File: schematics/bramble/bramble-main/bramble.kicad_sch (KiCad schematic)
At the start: 15 parts, among them Q1 DMN3300U, U1 TDN_5-0910WISM, U2 Opamp_Quad

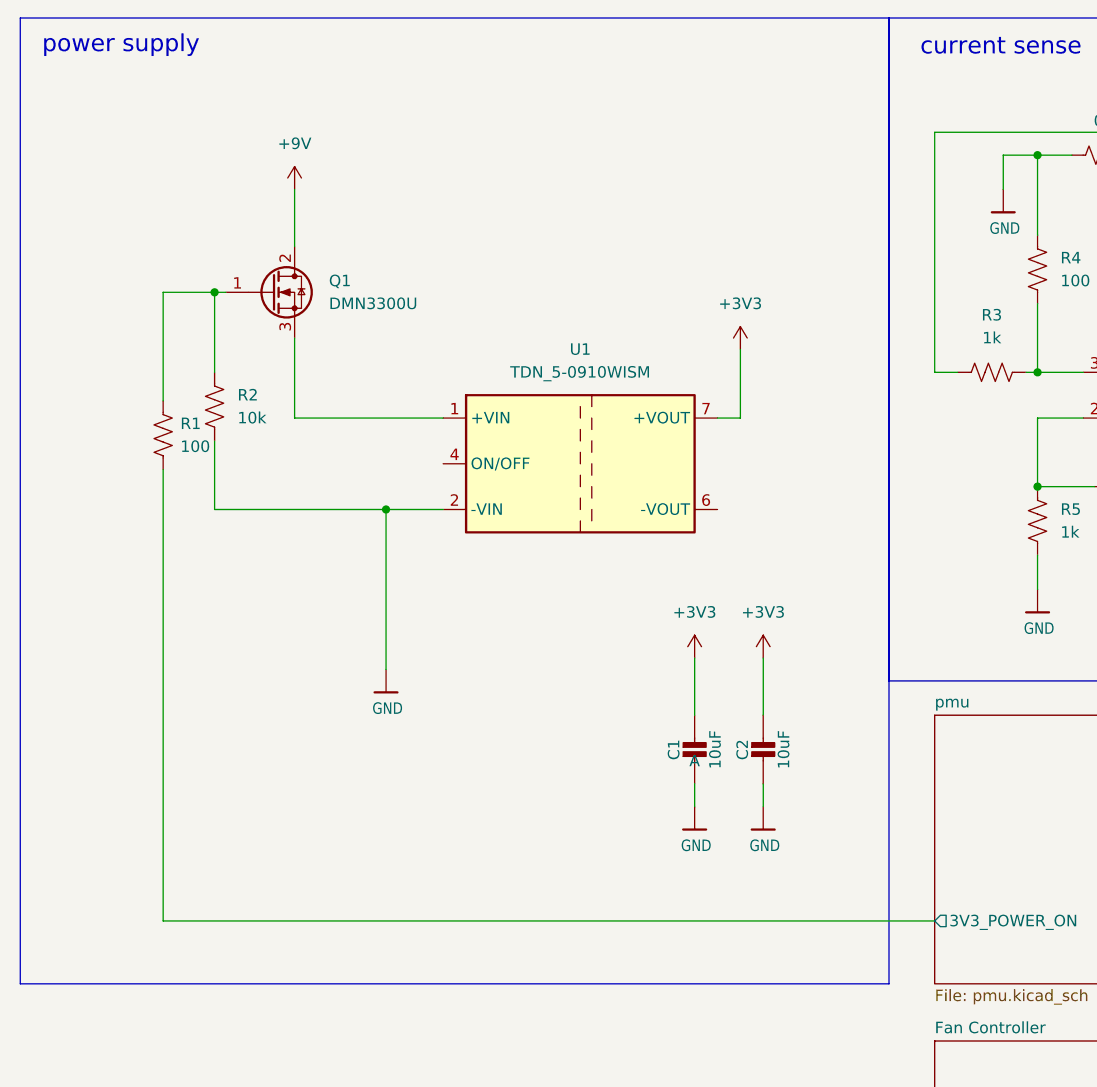
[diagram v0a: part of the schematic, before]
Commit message: fix: swap spi pins, change footprints, etc
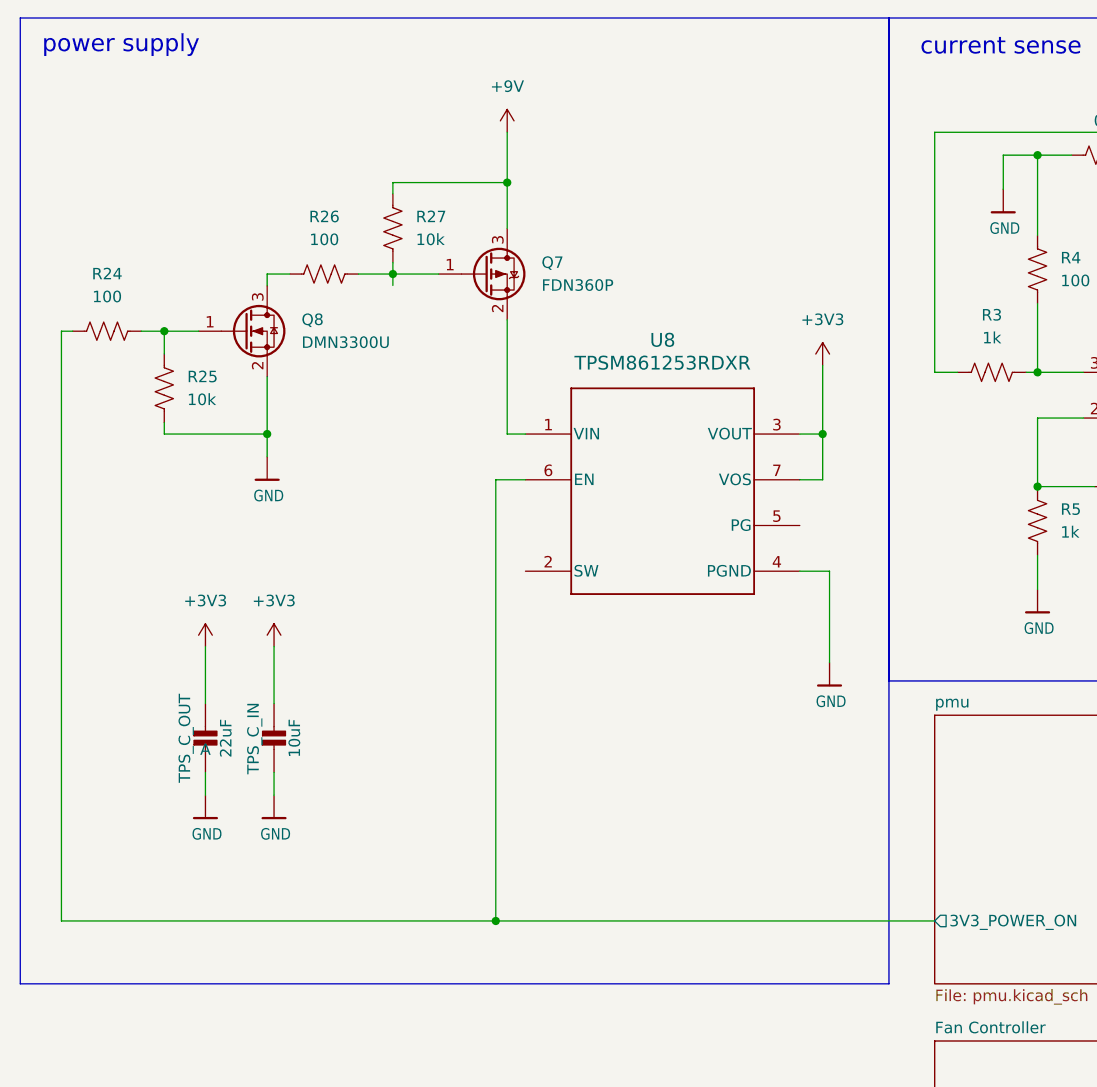
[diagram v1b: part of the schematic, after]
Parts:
- removed Q1: DMN3300U, Package_TO_SOT_SMD:SOT-23, symbol Transistor_FET:DMN3300U
- removed R1: 100, Resistor_SMD:R_0805_2012Metric, symbol Device:R_US
- removed R2: 10k, Resistor_SMD:R_0805_2012Metric, symbol Device:R_US
- removed U1: TDN_5-0910WISM, Converter_DCDC:Converter_DCDC_TRACO_TDN_5-xxxxWISM_SMD, symbol Regulator_Switching:TDN_5-0910WISM
- added Q7: FDN360P, Package_TO_SOT_SMD:SOT-23, symbol Transistor_FET:FDN340P
- added Q8: DMN3300U, Package_TO_SOT_SMD:SOT-23, symbol Transistor_FET:DMN3300U
- added R24: 100, Resistor_SMD:R_0805_2012Metric, symbol Device:R_US
- added R25: 10k, Resistor_SMD:R_0805_2012Metric, symbol Device:R_US
- added R26: 100, Capacitor_SMD:C_0805_2012Metric, symbol Device:R_US
- added R27: 10k, Capacitor_SMD:C_0805_2012Metric, symbol Device:R_US
- added U8: TPSM861253RDXR, RDX0007A-MFG, symbol TPSM861253RDXR:TPSM861253RDXR
- TPS_C_OUT: renamed from C1; value 10uF -> 22uF
- renumbered C2 to TPS_C_IN
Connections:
- net +3V3: now also U8.3 (VOUT), U8.7 (VOS)
- net +9V: now also Q7.3 (D), R27.1
- net GND: now also Q8.2 (S), R25.2, U8.4 (PGND)
- net pmu/3V3_POWER_ON: now also R24.2, U8.6 (EN)
- new net: Q8.1 (G), R24.1, R25.1
- new net: Q8.3 (D), R26.2
- new net: Q7.1 (G), R26.1, R27.2
- new net: Q7.2 (S), U8.1 (VIN)
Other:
- moved on the sheet: TPS_C_IN, TPS_C_OUT

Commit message: pre-fab check-in of v2
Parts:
- removed U8: TPSM861253RDXR, RDX0007A-MFG, symbol TPSM861253RDXR:TPSM861253RDXR
- added VR1: TPSM861253RDXR, Bramble:VREG_TPSM861253RDXR, symbol bramble:TPSM861253RDXR
- R3: renamed from R26; value 100 -> 100k
- renumbered Q8 to Q1, Q7 to Q2, R24 to R1, R8 to R10, R9 to R11, R10 to R12, R25 to R2, R27 to R4, R3 to R5, R4 to R6, R5 to R7, R6 to R8, R7 to R9, TPS_C_IN to TPS_C_IN1, TPS_C_OUT to TPS_C_OUT1
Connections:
- net +3V3: now also VR1.3 (VOUT), VR1.5 (PG)
- net GND: now also VR1.4 (PGND)
- net pmu/3V3_POWER_ON: now also VR1.6 (EN)
- net at Q2.2 (S): now also VR1.1 (VIN)
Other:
- removed sheet Fan Controller

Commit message: Checking before rollback
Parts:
- renumbered U2 to U1
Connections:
- net +3V3: now also VR1.7 (VOS); no longer VR1.5 (PG)
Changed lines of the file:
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@@
 	)
 	(junction
-		(at 31.242 50.038)
+		(at 104.394 61.468)
 		(diameter 0)
 		(color 0 0 0 0)
 	)
 	(junction
-		(at 128.27 67.31)
+		(at 31.242 50.038)
 		(diameter 0)
 		(color 0 0 0 0)
 	)
 	(junction
-		(at 104.394 61.468)
+		(at 128.27 67.31)
 		(diameter 0)
 		(color 0 0 0 0)
@@
 	(wire
 		(pts
-			(xy 203.2 58.42) (xy 199.39 58.42)
+			(xy 101.854 71.628) (xy 104.394 71.628)
 		)
 		(stroke
@@
 	(wire
 		(pts
-			(xy 101.854 61.468) (xy 104.394 61.468)
+			(xy 203.2 58.42) (xy 199.39 58.42)
 		)
 		(stroke
@@
 	(wire
 		(pts
-			(xy 104.394 66.548) (xy 104.394 61.468)
+			(xy 101.854 61.468) (xy 104.394 61.468)
 		)
 		(stroke
@@
 	(wire
 		(pts
+			(xy 104.394 61.468) (xy 104.394 71.628)
+		)
+		(stroke
+			(width 0)
+			(type default)
+		)
+	)
+	(wire
+		(pts
 			(xy 199.39 58.42) (xy 199.39 63.5)
 		)
@@
 	(wire
 		(pts
-			(xy 101.854 66.548) (xy 104.394 66.548)
+			(xy 104.394 53.848) (xy 104.394 61.468)
 		)
 		(stroke
@@
 	(wire
 		(pts
-			(xy 104.394 53.848) (xy 104.394 61.468)
-		)
-		(stroke
-			(width 0)
-			(type default)
-		)
-	)
-	(wire
-		(pts
 			(xy 42.672 61.468) (xy 42.672 64.008)
 		)
@@
 		(dnp no)
 		(fields_autoplaced yes)
-		(property "Reference" "U2"
+		(property "Reference" "U1"
 			(at 274.32 31.75 0)
 			(effects
@@
 			(project ""
 				(path "/e35d7dcf-51bd-456f-89cf-e52d660079b4"
-					(reference "U2")
+					(reference "U1")
 					(unit 3)
 				)
@@
 		(dnp no)
 		(fields_autoplaced yes)
-		(property "Reference" "U2"
+		(property "Reference" "U1"
 			(at 140.97 46.99 0)
 			(effects
@@
 			(project ""
 				(path "/e35d7dcf-51bd-456f-89cf-e52d660079b4"
-					(reference "U2")
+					(reference "U1")
 					(unit 1)
 				)
@@
 		(dnp no)
 		(fields_autoplaced yes)
-		(property "Reference" "U2"
+		(property "Reference" "U1"
 			(at 210.82 45.72 0)
 			(effects
@@
 			(project ""
 				(path "/e35d7dcf-51bd-456f-89cf-e52d660079b4"
-					(reference "U2")
+					(reference "U1")
 					(unit 2)
 				)
@@
 		(dnp no)
 		(fields_autoplaced yes)
-		(property "Reference" "U2"
+		(property "Reference" "U1"
 			(at 274.32 50.8 0)
 			(effects
@@
 			(project ""
 				(path "/e35d7dcf-51bd-456f-89cf-e52d660079b4"
-					(reference "U2")
+					(reference "U1")
 					(unit 4)
 				)
@@
 					(unit 1)
 				)
+				(path "/e35d7dcf-51bd-456f-89cf-e52d660079b4/df1d8afa-9717-44ff-901e-40cae4aada91"
+					(reference "VR1")
+					(unit 1)
+				)
 			)
 		)
@@
 		(dnp no)
 		(fields_autoplaced yes)
-		(property "Reference" "U2"
+		(property "Reference" "U1"
 			(at 252.73 48.2599 0)
 			(effects
@@
 			(project ""
 				(path "/e35d7dcf-51bd-456f-89cf-e52d660079b4"
-					(reference "U2")
+					(reference "U1")
 					(unit 5)
 				)

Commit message: Check in some of the v3 change
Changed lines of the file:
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@@
+	)
+	(junction
+		(at 104.394 61.468)
+		(diameter 0)
+		(color 0 0 0 0)
 	)
 	(junction
@@
 	)
 	(junction
-		(at 104.394 61.468)
-		(diameter 0)
-		(color 0 0 0 0)
-	)
-	(junction
 		(at 31.242 50.038)
 		(diameter 0)
@@
 	(wire
 		(pts
-			(xy 101.854 71.628) (xy 104.394 71.628)
-		)
-		(stroke
-			(width 0)
-			(type default)
-		)
-	)
-	(wire
-		(pts
 			(xy 203.2 58.42) (xy 199.39 58.42)
 		)
@@
 	(wire
 		(pts
-			(xy 104.394 61.468) (xy 104.394 71.628)
-		)
-		(stroke
-			(width 0)
-			(type default)
-		)
-	)
-	(wire
-		(pts
 			(xy 199.39 58.42) (xy 199.39 63.5)
 		)
@@
 	(wire
 		(pts
+			(xy 101.854 71.628) (xy 104.394 71.628)
+		)
+		(stroke
+			(width 0)
+			(type default)
+		)
+	)
+	(wire
+		(pts
 			(xy 160.02 83.82) (xy 228.6 83.82)
 		)
@@
 	(wire
 		(pts
+			(xy 43.434 85.09) (xy 43.434 91.44)
+		)
+		(stroke
+			(width 0)
+			(type default)
+		)
+	)
+	(wire
+		(pts
+			(xy 220.98 55.88) (xy 228.6 55.88)
+		)
+		(stroke
+			(width 0)
+			(type default)
+		)
+	)
+	(wire
+		(pts
+			(xy 56.642 33.528) (xy 69.342 33.528)
+		)
+		(stroke
+			(width 0)
+			(type default)
+		)
+	)
+	(wire
+		(pts
+			(xy 140.97 30.48) (xy 140.97 27.94)
+		)
+		(stroke
+			(width 0)
+			(type default)
+		)
+	)
+	(wire
+		(pts
+			(xy 163.83 57.15) (xy 166.37 57.15)
+		)
+		(stroke
+			(width 0)
+			(type default)
+		)
+	)
+	(wire
+		(pts
+			(xy 140.97 30.48) (xy 148.59 30.48)
+		)
+		(stroke
+			(width 0)
+			(type default)
+		)
+	)
+	(wire
+		(pts
+			(xy 35.814 85.09) (xy 35.814 91.44)
+		)
+		(stroke
+			(width 0)
+			(type default)
+		)
+	)
+	(wire
+		(pts
+			(xy 133.35 59.69) (xy 128.27 59.69)
+		)
+		(stroke
+			(width 0)
+			(type default)
+		)
+	)
+	(wire
+		(pts
+			(xy 153.67 67.31) (xy 153.67 57.15)
+		)
+		(stroke
+			(width 0)
+			(type default)
+		)
+	)
+	(wire
+		(pts
+			(xy 128.27 54.61) (xy 133.35 54.61)
+		)
+		(stroke
+			(width 0)
+			(type default)
+		)
+	)
+	(wire
+		(pts
+			(xy 175.26 99.06) (xy 176.53 99.06)
+		)
+		(stroke
+			(width 0)
+			(type default)
+		)
+	)
+	(wire
+		(pts
+			(xy 220.98 55.88) (xy 218.44 55.88)
+		)
+		(stroke
+			(width 0)
+			(type default)
+		)
+	)
+	(wire
+		(pts
+			(xy 190.5 41.91) (xy 190.5 44.45)
+		)
+		(stroke
+			(width 0)
+			(type default)
+		)
+	)
+	(wire
+		(pts
+			(xy 190.5 53.34) (xy 203.2 53.34)
+		)
+		(stroke
+			(width 0)
+			(type default)
+		)
+	)
+	(wire
+		(pts
+			(xy 128.27 59.69) (xy 128.27 67.31)
+		)
+		(stroke
+			(width 0)
+			(type default)
+		)
+	)
+	(wire
+		(pts
+			(xy 175.26 104.14) (xy 176.53 104.14)
+		)
+		(stroke
+			(width 0)
+			(type default)
+		)
+	)
+	(wire
+		(pts
+			(xy 128.27 46.99) (xy 128.27 54.61)
+		)
+		(stroke
+			(width 0)
+			(type default)
+		)
+	)
+	(wire
+		(pts
+			(xy 128.27 30.48) (xy 128.27 39.37)
+		)
+		(stroke
+			(width 0)
+			(type default)
+		)
+	)
+	(wire
+		(pts
+			(xy 104.394 71.628) (xy 104.394 61.468)
+		)
+		(stroke
+			(width 0)
+			(type default)
+		)
+	)
+	(wire
+		(pts
 			(xy 104.394 53.848) (xy 104.394 61.468)
-		)
-		(stroke
-			(width 0)
-			(type default)
-		)
-	)
-	(wire
-		(pts
-			(xy 43.434 85.09) (xy 43.434 91.44)
-		)
-		(stroke
-			(width 0)
-			(type default)
-		)
-	)
-	(wire
-		(pts
-			(xy 220.98 55.88) (xy 228.6 55.88)
-		)
-		(stroke
-			(width 0)
-			(type default)
-		)
-	)
-	(wire
-		(pts
-			(xy 56.642 33.528) (xy 69.342 33.528)
-		)
-		(stroke
-			(width 0)
-			(type default)
-		)
-	)
-	(wire
-		(pts
-			(xy 140.97 30.48) (xy 140.97 27.94)
-		)
-		(stroke
-			(width 0)
-			(type default)
-		)
-	)
-	(wire
-		(pts
-			(xy 163.83 57.15) (xy 166.37 57.15)
-		)
-		(stroke
-			(width 0)
-			(type default)
-		)
-	)
-	(wire
-		(pts
-			(xy 140.97 30.48) (xy 148.59 30.48)
-		)
-		(stroke
-			(width 0)
-			(type default)
-		)
-	)
-	(wire
-		(pts
-			(xy 35.814 85.09) (xy 35.814 91.44)
-		)
-		(stroke
-			(width 0)
-			(type default)
-		)
-	)
-	(wire
-		(pts
-			(xy 133.35 59.69) (xy 128.27 59.69)
-		)
-		(stroke
-			(width 0)
-			(type default)
-		)
-	)
-	(wire
-		(pts
-			(xy 153.67 67.31) (xy 153.67 57.15)
-		)
-		(stroke
-			(width 0)
-			(type default)
-		)
-	)
-	(wire
-		(pts
-			(xy 128.27 54.61) (xy 133.35 54.61)
-		)
-		(stroke
-			(width 0)
-			(type default)
-		)
-	)
-	(wire
-		(pts
-			(xy 175.26 99.06) (xy 176.53 99.06)
-		)
-		(stroke
-			(width 0)
-			(type default)
-		)
-	)
-	(wire
-		(pts
-			(xy 220.98 55.88) (xy 218.44 55.88)
-		)
-		(stroke
-			(width 0)
-			(type default)
-		)
-	)
-	(wire
-		(pts
-			(xy 190.5 41.91) (xy 190.5 44.45)
-		)
-		(stroke
-			(width 0)
-			(type default)
-		)
-	)
-	(wire
-		(pts
-			(xy 190.5 53.34) (xy 203.2 53.34)
-		)
-		(stroke
-			(width 0)
-			(type default)
-		)
-	)
-	(wire
-		(pts
-			(xy 128.27 59.69) (xy 128.27 67.31)
-		)
-		(stroke
-			(width 0)
-			(type default)
-		)
-	)
-	(wire
-		(pts
-			(xy 175.26 104.14) (xy 176.53 104.14)
-		)
-		(stroke
-			(width 0)
-			(type default)
-		)
-	)
-	(wire
-		(pts
-			(xy 128.27 46.99) (xy 128.27 54.61)
-		)
-		(stroke
-			(width 0)
-			(type default)
-		)
-	)
-	(wire
-		(pts
-			(xy 128.27 30.48) (xy 128.27 39.37)
 		)
 		(stroke
@@
 					(reference "VR1")
 					(unit 1)
-				)
-				(path "/e35d7dcf-51bd-456f-89cf-e52d660079b4/df1d8afa-9717-44ff-901e-40cae4aada91"
-					(reference "VR1")
-					(unit 1)

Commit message: Remove mosfet switching from design: new dcdc is fine alone
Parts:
- removed Q1: DMN3300U, Package_TO_SOT_SMD:SOT-23, symbol Transistor_FET:DMN3300U
- removed Q2: FDN360P, Package_TO_SOT_SMD:SOT-23, symbol Transistor_FET:FDN340P
- removed R1: 100, Resistor_SMD:R_0805_2012Metric, symbol Device:R_US
- removed R2: 10k, Resistor_SMD:R_0805_2012Metric, symbol Device:R_US
- removed R3: 100k, Capacitor_SMD:C_0805_2012Metric, symbol Device:R_US
- removed R4: 10k, Capacitor_SMD:C_0805_2012Metric, symbol Device:R_US
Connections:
- net +9V: now also VR1.1 (VIN)
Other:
- moved on the sheet: VR1

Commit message: Add test pads
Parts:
- added TP6: 3V3 TEST, TestPoint:TestPoint_Pad_1.5x1.5mm, symbol Connector:TestPoint
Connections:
- net +3V3: now also TP6.1
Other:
- company: (none) -> Barefoot Systems
- title: (none) -> Bramble
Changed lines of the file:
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@@
 	(generator_version "9.0")
 	(paper "A4")
+	(title_block
+		(title "Bramble")
+		(date "2026-01-24")
+		(rev "v4")
+		(company "Barefoot Systems")
+	)
 	(rectangle
 		(start 15.24 15.24)
@@
 	(wire
 		(pts
+			(xy 98.806 55.118) (xy 98.806 61.468)
+		)
+		(stroke
+			(width 0)
+			(type default)
+		)
+	)
+	(wire
+		(pts
 			(xy 228.6 55.88) (xy 228.6 83.82)
 		)
@@
 		(pts
 			(xy 59.944 61.468) (xy 61.976 61.468)
+		)
+		(stroke
+			(width 0)
+			(type default)
+		)
+	)
+	(wire
+		(pts
+			(xy 94.996 61.468) (xy 98.806 61.468)
 		)
 		(stroke
@@
 					(unit 1)
 				)
+			)
+		)
+	)
+	(symbol
+		(lib_id "Connector:TestPoint")
+		(at 98.806 55.118 0)
+		(unit 1)
+		(exclude_from_sim no)
+		(in_bom yes)
+		(on_board yes)
+		(dnp no)
+		(fields_autoplaced yes)
+		(property "Reference" "TP6"
+			(at 100.33 50.5459 0)
+			(effects
+				(font
+					(size 1.27 1.27)
+				)
+				(justify left)
+			)
+		)
+		(property "Value" "3V3 TEST"
+			(at 100.33 53.0859 0)
+			(effects
+				(font
+					(size 1.27 1.27)
+				)
+				(justify left)
+			)
+		)
+		(property "Footprint" "TestPoint:TestPoint_Pad_1.5x1.5mm"
+			(at 103.886 55.118 0)
+			(effects
+				(font
+					(size 1.27 1.27)
+				)
+				(hide yes)
+			)
+		)
+		(property "Datasheet" "~"
+			(at 103.886 55.118 0)
+			(effects
+				(font
+					(size 1.27 1.27)
+				)
+				(hide yes)
+			)
+		)
+		(property "Description" "test point"
+			(at 98.806 55.118 0)
+			(effects
+				(font
+					(size 1.27 1.27)
+				)
+				(hide yes)
+			)
+		)
+		(pin "1"
+		)
+		(instances
+			(project ""
+				(path "/e35d7dcf-51bd-456f-89cf-e52d660079b4"
+					(reference "TP6")
+					(unit 1)
+				)

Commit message: Checking in v4 schematic/board prior to attempting jlcpcb run
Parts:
- removed TPS_C_IN1: 10uF, Capacitor_SMD:C_0805_2012Metric, symbol Adafruit Feather RP2040 RFM-eagle-import:CAP_CERAMIC0805-NOOUTLINE
- removed TPS_C_OUT1: 22uF, Capacitor_SMD:C_0805_2012Metric, symbol Adafruit Feather RP2040 RFM-eagle-import:CAP_CERAMIC0805-NOOUTLINE
- added C1: 10uF, Capacitor_SMD:C_0805_2012Metric, symbol Device:C
- added C2: 22uF, Capacitor_SMD:C_0805_2012Metric, symbol Device:C
- renumbered R5 to R1, R6 to R2, R7 to R3, R8 to R4, R9 to R5, R10 to R6, R11 to R7, R12 to R8, TP6 to TP1
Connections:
- net +3V3: now also C1.1, C2.1
- net GND: now also C1.2, C2.2
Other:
- sheet rp2040 renamed rp2350B (page 4)
- moved on the sheet: TP1, VR1
